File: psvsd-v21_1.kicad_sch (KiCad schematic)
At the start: 4 parts, among them U2 3.3V

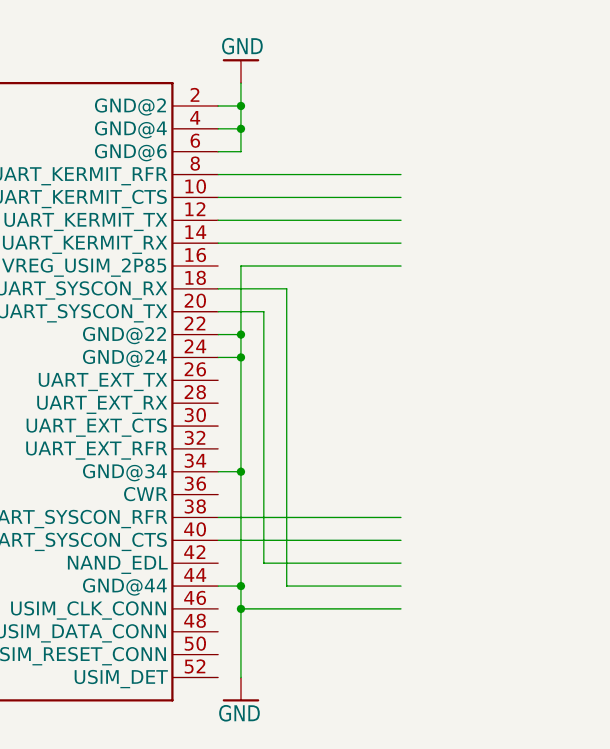
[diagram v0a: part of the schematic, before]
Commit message: Add UART and SWDIO debug headers (plus delete some accidental junk files)
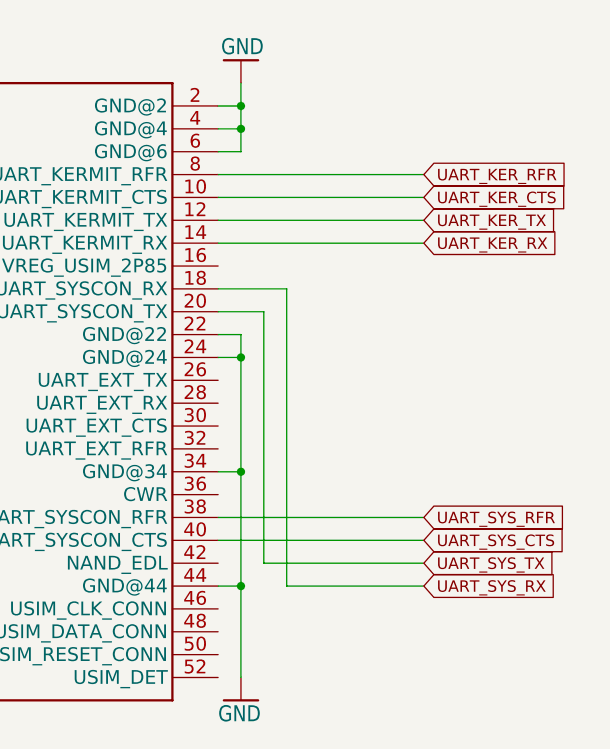
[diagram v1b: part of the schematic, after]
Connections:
- net UART_KER_CTS: now reaches U$1.10 (UART_KERMIT_CTS)
- net UART_KER_TX: now reaches U$1.12 (UART_KERMIT_TX)
- net UART_KER_RX: now reaches U$1.14 (UART_KERMIT_RX)
- net UART_SYS_RX: now reaches U$1.18 (UART_SYSCON_RX)
- net UART_SYS_TX: now reaches U$1.20 (UART_SYSCON_TX)
- net UART_SYS_RFR: now reaches U$1.38 (UART_SYSCON_RFR)
- net UART_SYS_CTS: now reaches U$1.40 (UART_SYSCON_CTS)
- net UART_KER_RFR: now reaches U$1.8 (UART_KERMIT_RFR)
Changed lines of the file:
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@@
-	)
-	(junction
-		(at 205.74 137.16)
-		(diameter 0)
-		(color 0 0 0 0)
 	)
 	(junction
@@
 	)
 	(junction
-		(at 205.74 106.68)
-		(diameter 0)
-		(color 0 0 0 0)
-	)
-	(junction
 		(at 205.74 109.22)
 		(diameter 0)
@@
 	(wire
 		(pts
-			(xy 223.52 99.06) (xy 205.74 99.06)
-		)
-		(stroke
-			(width 0.1524)
-			(type solid)
-		)
-	)
-	(wire
-		(pts
 			(xy 134.62 132.08) (xy 132.08 132.08)
 		)
@@
 	(wire
 		(pts
-			(xy 205.74 134.62) (xy 205.74 137.16)
-		)
-		(stroke
-			(width 0.1524)
-			(type solid)
-		)
-	)
-	(wire
-		(pts
-			(xy 203.2 91.44) (xy 223.52 91.44)
+			(xy 203.2 91.44) (xy 226.06 91.44)
 		)
 		(stroke
@@
 	(wire
 		(pts
-			(xy 203.2 129.54) (xy 223.52 129.54)
-		)
-		(stroke
-			(width 0.1524)
-			(type solid)
-		)
-	)
-	(wire
-		(pts
-			(xy 203.2 88.9) (xy 223.52 88.9)
+			(xy 203.2 129.54) (xy 226.06 129.54)
+		)
+		(stroke
+			(width 0.1524)
+			(type solid)
+		)
+	)
+	(wire
+		(pts
+			(xy 203.2 88.9) (xy 226.06 88.9)
 		)
 		(stroke
@@
 	(wire
 		(pts
-			(xy 203.2 127) (xy 223.52 127)
+			(xy 203.2 127) (xy 226.06 127)
 		)
 		(stroke
@@
 	(wire
 		(pts
-			(xy 223.52 132.08) (xy 208.28 132.08)
+			(xy 208.28 132.08) (xy 226.06 132.08)
 		)
 		(stroke
@@
 	(wire
 		(pts
-			(xy 223.52 134.62) (xy 210.82 134.62)
+			(xy 210.82 134.62) (xy 226.06 134.62)
 		)
 		(stroke
@@
 	(wire
 		(pts
-			(xy 205.74 99.06) (xy 205.74 106.68)
-		)
-		(stroke
-			(width 0.1524)
-			(type solid)
-		)
-	)
-	(wire
-		(pts
 			(xy 203.2 106.68) (xy 205.74 106.68)
 		)
@@
 	(wire
 		(pts
-			(xy 203.2 93.98) (xy 223.52 93.98)
+			(xy 203.2 93.98) (xy 226.06 93.98)
 		)
 		(stroke
@@
 	(wire
 		(pts
-			(xy 205.74 137.16) (xy 205.74 144.78)
+			(xy 205.74 134.62) (xy 205.74 144.78)
 		)
 		(stroke
@@
 	(wire
 		(pts
-			(xy 223.52 137.16) (xy 205.74 137.16)
-		)
-		(stroke
-			(width 0.1524)
-			(type solid)
-		)
-	)
-	(wire
-		(pts
 			(xy 132.08 137.16) (xy 132.08 134.62)
 		)
@@
 	(wire
 		(pts
-			(xy 203.2 96.52) (xy 223.52 96.52)
+			(xy 203.2 96.52) (xy 226.06 96.52)
 		)
 		(stroke
@@
 			(width 0.1524)
 			(type solid)
+		)
+	)
+	(global_label "UART_KER_CTS"
+		(shape input)
+		(at 226.06 91.44 0)
+		(fields_autoplaced yes)
+		(effects
+			(font
+				(size 1.27 1.27)
+			)
+			(justify left)
+		)
+		(property "Intersheetrefs" "${INTERSHEET_REFS}"
+			(at 241.5032 91.44 0)
+			(hide yes)
+			(show_name no)
+			(do_not_autoplace no)
+			(effects
+				(font
+					(size 1.27 1.27)
+				)
+				(justify left)
+			)
+		)
+	)
+	(global_label "UART_SYS_RFR"
+		(shape input)
+		(at 226.06 127 0)
+		(fields_autoplaced yes)
+		(effects
+			(font
+				(size 1.27 1.27)
+			)
+			(justify left)
+		)
+		(property "Intersheetrefs" "${INTERSHEET_REFS}"
+			(at 241.6242 127 0)
+			(hide yes)
+			(show_name no)
+			(do_not_autoplace no)
+			(effects
+				(font
+					(size 1.27 1.27)
+				)
+				(justify left)
+			)
+		)
+	)
+	(global_label "UART_KER_RFR"
+		(shape input)
+		(at 226.06 88.9 0)
+		(fields_autoplaced yes)
+		(effects
+			(font
+				(size 1.27 1.27)
+			)
+			(justify left)
+		)
+		(property "Intersheetrefs" "${INTERSHEET_REFS}"
+			(at 241.8056 88.9 0)
+			(hide yes)
+			(show_name no)
+			(do_not_autoplace no)
+			(effects
+				(font
+					(size 1.27 1.27)
+				)
+				(justify left)
+			)
 		)
 	)
@@
 		)
 	)
+	(global_label "UART_SYS_TX"
+		(shape input)
+		(at 226.06 132.08 0)
+		(fields_autoplaced yes)
+		(effects
+			(font
+				(size 1.27 1.27)
+			)
+			(justify left)
+		)
+		(property "Intersheetrefs" "${INTERSHEET_REFS}"
+			(at 242.5918 132.08 0)
+			(hide yes)
+			(show_name no)
+			(do_not_autoplace no)
+			(effects
+				(font
+					(size 1.27 1.27)
+				)
+				(justify left)
+			)
+		)
+	)
+	(global_label "UART_SYS_CTS"
+		(shape input)
+		(at 226.06 129.54 0)
+		(fields_autoplaced yes)
+		(effects
+			(font
+				(size 1.27 1.27)
+			)
+			(justify left)
+		)
+		(property "Intersheetrefs" "${INTERSHEET_REFS}"
+			(at 241.3218 129.54 0)
+			(hide yes)
+			(show_name no)
+			(do_not_autoplace no)
+			(effects
+				(font
+					(size 1.27 1.27)
+				)
+				(justify left)
+			)
+		)
+	)
+	(global_label "UART_SYS_RX"
+		(shape input)
+		(at 226.06 134.62 0)
+		(fields_autoplaced yes)
+		(effects
+			(font
+				(size 1.27 1.27)
+			)
+			(justify left)
+		)
+		(property "Intersheetrefs" "${INTERSHEET_REFS}"
+			(at 242.7733 134.62 0)
+			(hide yes)
+			(show_name no)
+			(do_not_autoplace no)
+			(effects
+				(font
+					(size 1.27 1.27)
+				)
+				(justify left)
+			)
+		)
+	)
 	(global_label "USB_N"
 		(shape bidirectional)
@@
 			)
 		)
+	)
+	(global_label "UART_KER_RX"
+		(shape input)
+		(at 226.06 96.52 0)
+		(fields_autoplaced yes)
+		(effects
+			(font
+				(size 1.27 1.27)
+			)
+			(justify left)
+		)
+		(property "Intersheetrefs" "${INTERSHEET_REFS}"
+			(at 242.9547 96.52 0)
+			(hide yes)
+			(show_name no)
+			(do_not_autoplace no)
+			(effects
+				(font
+					(size 1.27 1.27)
+				)
+				(justify left)
+			)
+		)
+	)
+	(global_label "UART_KER_TX"
+		(shape input)
+		(at 226.06 93.98 0)
+		(fields_autoplaced yes)
+		(effects
+			(font
+				(size 1.27 1.27)
+			)
+			(justify left)
+		)
+		(property "Intersheetrefs" "${INTERSHEET_REFS}"
+			(at 242.7732 93.98 0)
+			(hide yes)
+			(show_name no)
+			(do_not_autoplace no)
+			(effects
+				(font
+					(size 1.27 1.27)
+				)
+				(justify left)
+			)
+		)

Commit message: Fix wrong resistor package
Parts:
- C10, C9: footprint Footprints:C0603_464 -> Capacitor_SMD:C_01005_0402Metric
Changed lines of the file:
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@@
 			)
 		)
-		(property "Footprint" "Footprints:C0603_464"
+		(property "Footprint" "Capacitor_SMD:C_01005_0402Metric"
 			(at 66.04 127 0)
 			(hide yes)
@@
 			)
 		)
-		(property "Footprint" "Footprints:C0603_464"
+		(property "Footprint" "Capacitor_SMD:C_01005_0402Metric"
 			(at 99.06 127 0)
 			(hide yes)

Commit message: Improved layout to reduce reflections
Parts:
- added D2: CD0603-B0340R, symbol Device:D_Schottky
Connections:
- net VDD33: now also D2.1 (K); no longer C9.1, U2.5 (VOUT)
- new net: C9.1, D2.2 (A), U2.5 (VOUT)
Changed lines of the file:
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@@
+	)
+	(junction
+		(at 132.08 96.52)
+		(diameter 0)
+		(color 0 0 0 0)
 	)
 	(junction
@@
 	)
 	(junction
-		(at 132.08 96.52)
-		(diameter 0)
-		(color 0 0 0 0)
-	)
-	(junction
 		(at 99.06 121.92)
 		(diameter 0)
@@
 	(wire
 		(pts
-			(xy 134.62 83.82) (xy 132.08 83.82)
-		)
-		(stroke
-			(width 0.1524)
-			(type solid)
-		)
-	)
-	(wire
-		(pts
-			(xy 203.2 129.54) (xy 226.06 129.54)
-		)
-		(stroke
-			(width 0.1524)
-			(type solid)
-		)
-	)
-	(wire
-		(pts
-			(xy 203.2 88.9) (xy 226.06 88.9)
-		)
-		(stroke
-			(width 0.1524)
-			(type solid)
-		)
-	)
-	(wire
-		(pts
-			(xy 203.2 109.22) (xy 205.74 109.22)
-		)
-		(stroke
-			(width 0.1524)
-			(type solid)
-		)
-	)
-	(wire
-		(pts
-			(xy 132.08 127) (xy 132.08 124.46)
-		)
-		(stroke
-			(width 0.1524)
-			(type solid)
-		)
-	)
-	(wire
-		(pts
-			(xy 66.04 130.81) (xy 66.04 132.08)
+			(xy 63.5 121.92) (xy 66.04 121.92)
 		)
 		(stroke
@@
 	(wire
 		(pts
-			(xy 134.62 106.68) (xy 132.08 106.68)
-		)
-		(stroke
-			(width 0.1524)
-			(type solid)
-		)
-	)
-	(wire
-		(pts
-			(xy 149.86 66.04) (xy 149.86 68.58)
-		)
-		(stroke
-			(width 0.1524)
-			(type solid)
-		)
-	)
-	(wire
-		(pts
-			(xy 208.28 132.08) (xy 208.28 104.14)
-		)
-		(stroke
-			(width 0.1524)
-			(type solid)
-		)
-	)
-	(wire
-		(pts
-			(xy 132.08 144.78) (xy 132.08 142.24)
-		)
-		(stroke
-			(width 0.1524)
-			(type solid)
-		)
-	)
-	(wire
-		(pts
-			(xy 132.08 139.7) (xy 132.08 137.16)
-		)
-		(stroke
-			(width 0.1524)
-			(type solid)
-		)
-	)
-	(wire
-		(pts
-			(xy 132.08 81.28) (xy 132.08 78.74)
-		)
-		(stroke
-			(width 0.1524)
-			(type solid)
-		)
-	)
-	(wire
-		(pts
-			(xy 66.04 121.92) (xy 76.2 121.92)
-		)
-		(stroke
-			(width 0.1524)
-			(type solid)
-		)
-	)
-	(wire
-		(pts
-			(xy 134.62 142.24) (xy 132.08 142.24)
-		)
-		(stroke
-			(width 0.1524)
-			(type solid)
-		)
-	)
-	(wire
-		(pts
-			(xy 58.42 121.92) (xy 66.04 121.92)
+			(xy 134.62 83.82) (xy 132.08 83.82)
+		)
+		(stroke
+			(width 0.1524)
+			(type solid)
+		)
+	)
+	(wire
+		(pts
+			(xy 203.2 129.54) (xy 226.06 129.54)
+		)
+		(stroke
+			(width 0.1524)
+			(type solid)
+		)
+	)
+	(wire
+		(pts
+			(xy 203.2 88.9) (xy 226.06 88.9)
+		)
+		(stroke
+			(width 0.1524)
+			(type solid)
+		)
+	)
+	(wire
+		(pts
+			(xy 203.2 109.22) (xy 205.74 109.22)
+		)
+		(stroke
+			(width 0.1524)
+			(type solid)
+		)
+	)
+	(wire
+		(pts
+			(xy 132.08 127) (xy 132.08 124.46)
+		)
+		(stroke
+			(width 0.1524)
+			(type solid)
+		)
+	)
+	(wire
+		(pts
+			(xy 66.04 130.81) (xy 66.04 132.08)
 		)
 		(stroke
@@
 	(wire
 		(pts
+			(xy 134.62 106.68) (xy 132.08 106.68)
+		)
+		(stroke
+			(width 0.1524)
+			(type solid)
+		)
+	)
+	(wire
+		(pts
+			(xy 149.86 66.04) (xy 149.86 68.58)
+		)
+		(stroke
+			(width 0.1524)
+			(type solid)
+		)
+	)
+	(wire
+		(pts
+			(xy 208.28 132.08) (xy 208.28 104.14)
+		)
+		(stroke
+			(width 0.1524)
+			(type solid)
+		)
+	)
+	(wire
+		(pts
+			(xy 132.08 144.78) (xy 132.08 142.24)
+		)
+		(stroke
+			(width 0.1524)
+			(type solid)
+		)
+	)
+	(wire
+		(pts
+			(xy 132.08 139.7) (xy 132.08 137.16)
+		)
+		(stroke
+			(width 0.1524)
+			(type solid)
+		)
+	)
+	(wire
+		(pts
+			(xy 132.08 81.28) (xy 132.08 78.74)
+		)
+		(stroke
+			(width 0.1524)
+			(type solid)
+		)
+	)
+	(wire
+		(pts
+			(xy 66.04 121.92) (xy 76.2 121.92)
+		)
+		(stroke
+			(width 0.1524)
+			(type solid)
+		)
+	)
+	(wire
+		(pts
+			(xy 134.62 142.24) (xy 132.08 142.24)
+		)
+		(stroke
+			(width 0.1524)
+			(type solid)
+		)
+	)
+	(wire
+		(pts
 			(xy 203.2 127) (xy 226.06 127)
 		)
@@
 			(width 0.1524)
 			(type solid)
+		)
+	)
+	(wire
+		(pts
+			(xy 53.34 121.92) (xy 55.88 121.92)
+		)
+		(stroke
+			(width 0)
+			(type default)
 		)
 	)
@@
 	(global_label "VDD33"
 		(shape bidirectional)
-		(at 58.42 121.92 180)
+		(at 53.34 121.92 180)
 		(fields_autoplaced yes)
 		(effects
@@
 		)
 		(property "Intersheetrefs" "${INTERSHEET_REFS}"
-			(at 48.4792 121.92 0)
+			(at 43.3992 121.92 0)
 			(hide yes)
 			(show_name no)
@@
 					(unit 1)
 				)
+			)
+		)
+	)
+	(symbol
+		(lib_id "Device:D_Schottky")
+		(at 59.69 121.92 0)
+		(unit 1)
+		(body_style 1)
+		(exclude_from_sim no)
+		(in_bom yes)
+		(on_board yes)
+		(in_pos_files yes)
+		(dnp no)
+		(fields_autoplaced yes)
+		(property "Reference" "D2"
+			(at 59.3725 115.57 0)
+			(show_name no)
+			(do_not_autoplace no)
+			(effects
+				(font
+					(size 1.27 1.27)
+				)
+			)
+		)
+		(property "Value" "CD0603-B0340R"
+			(at 59.3725 118.11 0)
+			(show_name no)
+			(do_not_autoplace no)
+			(effects
+				(font
+					(size 1.27 1.27)
+				)
+			)
+		)
+		(property "Footprint" ""
+			(at 59.69 121.92 0)
+			(hide yes)
+			(show_name no)
+			(do_not_autoplace no)
+			(effects
+				(font
+					(size 1.27 1.27)
+				)
+			)
+		)
+		(property "Datasheet" ""
+			(at 59.69 121.92 0)
+			(hide yes)
+			(show_name no)
+			(do_not_autoplace no)
+			(effects
+				(font
+					(size 1.27 1.27)
+				)
+			)
+		)
+		(property "Description" "Schottky diode"
+			(at 59.69 121.92 0)
+			(hide yes)
+			(show_name no)
+			(do_not_autoplace no)
+			(effects
+				(font
+					(size 1.27 1.27)
+				)
+			)
+		)
+		(pin "1"
+		)
+		(pin "2"
+		)
+		(instances
+			(project "psvsd"
+				(path "/4e154789-230f-48f5-8bce-af12a707c6dc/314dc8a3-d23a-4868-9b71-fad4ce898ab2"
+					(reference "D2")
+					(unit 1)
+				)

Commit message: Added external 3.3v supply for debug (with backflow diodes)
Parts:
- D2: footprint (none) -> Diode_SMD:D_0603_1608Metric
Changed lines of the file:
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@@
 			)
 		)
-		(property "Footprint" ""
+		(property "Footprint" "Diode_SMD:D_0603_1608Metric"
 			(at 59.69 121.92 0)
 			(hide yes)

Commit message: Increased size of footprints to comply with more fab houses.
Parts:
- C10, C9: footprint Capacitor_SMD:C_01005_0402Metric -> Capacitor_SMD:C_0402_1005Metric_Pad0.74x0.62mm_HandSolder
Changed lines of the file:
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@@
 			)
 		)
-		(property "Footprint" "Capacitor_SMD:C_01005_0402Metric"
+		(property "Footprint" "Capacitor_SMD:C_0402_1005Metric_Pad0.74x0.62mm_HandSolder"
 			(at 66.04 127 0)
 			(hide yes)
@@
 			)
 		)
-		(property "Footprint" "Capacitor_SMD:C_01005_0402Metric"
+		(property "Footprint" "Capacitor_SMD:C_0402_1005Metric_Pad0.74x0.62mm_HandSolder"
 			(at 99.06 127 0)
 			(hide yes)
